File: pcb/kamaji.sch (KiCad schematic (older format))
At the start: 30 parts, among them J1 RJ10, J2 RJ10, J3 RJ10, J4 RJ10, J5 RJ10, Q1 IRF540N, SW1 CTRL1, SW2 CTRL2, SW3 CTRL3, U1 ATMEGA328P-PU

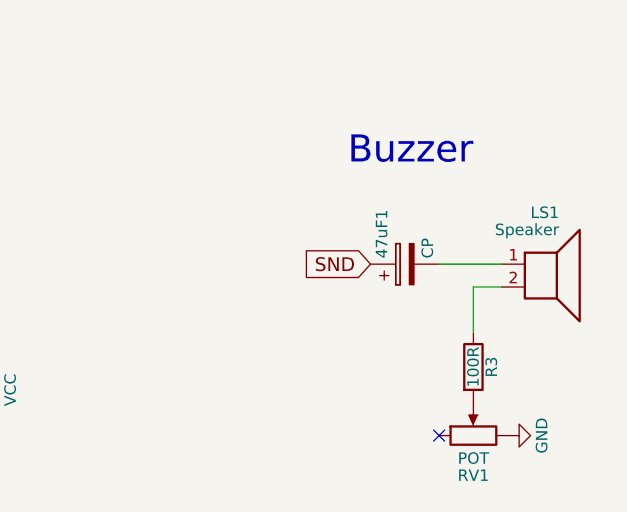
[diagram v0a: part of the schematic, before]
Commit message: fix the capacitor labels
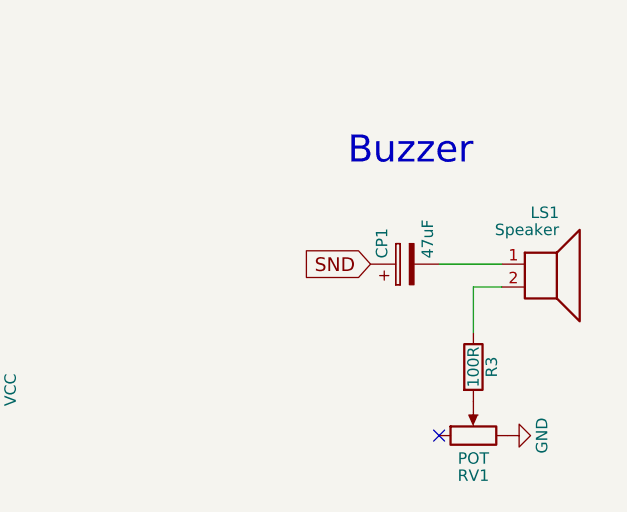
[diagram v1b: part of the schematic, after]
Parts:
- CP1: renamed from 47uF1; value CP -> 47uF
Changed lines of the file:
@@
 $EndComp
 $Comp
-L GND #PWR01
+L GND #PWR8
 U 1 1 596B2D5F
 P 2125 6925
-F 0 "#PWR01" H 2125 6675 50  0001 C CNN
+F 0 "#PWR8" H 2125 6675 50  0001 C CNN
 F 1 "GND" H 2125 6775 50  0000 C CNN
 F 2 "" H 2125 6925 50  0001 C CNN
@@
 $EndComp
 $Comp
-L GND #PWR02
+L GND #PWR7
 U 1 1 596B2D7D
 P 1950 6925
-F 0 "#PWR02" H 1950 6675 50  0001 C CNN
+F 0 "#PWR7" H 1950 6675 50  0001 C CNN
 F 1 "GND" H 1950 6775 50  0000 C CNN
 F 2 "" H 1950 6925 50  0001 C CNN
@@
 PBTN1
 $Comp
-L GND #PWR03
+L GND #PWR5
 U 1 1 596B3698
 P 1150 3925
-F 0 "#PWR03" H 1150 3675 50  0001 C CNN
+F 0 "#PWR5" H 1150 3675 50  0001 C CNN
 F 1 "GND" H 1150 3775 50  0000 C CNN
 F 2 "" H 1150 3925 50  0001 C CNN
@@
 $EndComp
 $Comp
-L VCC #PWR04
+L VCC #PWR32
 U 1 1 596B3963
 P 7275 4900
-F 0 "#PWR04" H 7275 4750 50  0001 C CNN
+F 0 "#PWR32" H 7275 4750 50  0001 C CNN
 F 1 "VCC" H 7275 5050 50  0000 C CNN
 F 2 "" H 7275 4900 50  0001 C CNN
@@
 $EndComp
 $Comp
-L VCC #PWR05
+L VCC #PWR6
 U 1 1 596B398D
 P 1175 1375
-F 0 "#PWR05" H 1175 1225 50  0001 C CNN
+F 0 "#PWR6" H 1175 1225 50  0001 C CNN
 F 1 "VCC" H 1175 1525 50  0000 C CNN
 F 2 "" H 1175 1375 50  0001 C CNN
@@
 $EndComp
 $Comp
-L GND #PWR06
+L GND #PWR30
 U 1 1 596B8372
 P 6975 5600
-F 0 "#PWR06" H 6975 5350 50  0001 C CNN
+F 0 "#PWR30" H 6975 5350 50  0001 C CNN
 F 1 "GND" H 6975 5450 50  0000 C CNN
 F 2 "" H 6975 5600 50  0001 C CNN
@@
 SND
 $Comp
-L GND #PWR07
+L GND #PWR35
 U 1 1 596BC371
 P 9650 5025
-F 0 "#PWR07" H 9650 4775 50  0001 C CNN
+F 0 "#PWR35" H 9650 4775 50  0001 C CNN
 F 1 "GND" H 9650 4875 50  0000 C CNN
 F 2 "" H 9650 5025 50  0001 C CNN
@@
 NoConn ~ 10050 4625
 $Comp
-L VCC #PWR08
+L VCC #PWR38
 U 1 1 596BC751
 P 10050 4425
-F 0 "#PWR08" H 10050 4275 50  0001 C CNN
+F 0 "#PWR38" H 10050 4275 50  0001 C CNN
 F 1 "VCC" H 10050 4575 50  0000 C CNN
 F 2 "" H 10050 4425 50  0001 C CNN
@@
 $EndComp
 $Comp
-L GND #PWR09
+L GND #PWR10
 U 1 1 596BE03C
 P 2875 5175
-F 0 "#PWR09" H 2875 4925 50  0001 C CNN
+F 0 "#PWR10" H 2875 4925 50  0001 C CNN
 F 1 "GND" H 2875 5025 50  0000 C CNN
 F 2 "" H 2875 5175 50  0001 C CNN
@@
 MOSI
 $Comp
-L VCC #PWR010
+L VCC #PWR9
 U 1 1 596BDF58
 P 2875 4850
-F 0 "#PWR010" H 2875 4700 50  0001 C CNN
+F 0 "#PWR9" H 2875 4700 50  0001 C CNN
 F 1 "VCC" H 2875 5000 50  0000 C CNN
 F 2 "" H 2875 4850 50  0001 C CNN
@@
 $EndComp
 $Comp
-L VCC #PWR011
+L VCC #PWR14
 U 1 1 596BDA9E
 P 4225 3400
-F 0 "#PWR011" H 4225 3250 50  0001 C CNN
+F 0 "#PWR14" H 4225 3250 50  0001 C CNN
 F 1 "VCC" H 4225 3550 50  0000 C CNN
 F 2 "" H 4225 3400 50  0001 C CNN
@@
 CBTN1
 $Comp
-L GND #PWR012
+L GND #PWR16
 U 1 1 596C3F76
 P 5125 4625
-F 0 "#PWR012" H 5125 4375 50  0001 C CNN
+F 0 "#PWR16" H 5125 4375 50  0001 C CNN
 F 1 "GND" H 5125 4475 50  0000 C CNN
 F 2 "" H 5125 4625 50  0001 C CNN
@@
 $EndComp
 $Comp
-L GND #PWR013
+L GND #PWR17
 U 1 1 596C4178
 P 5125 4925
-F 0 "#PWR013" H 5125 4675 50  0001 C CNN
+F 0 "#PWR17" H 5125 4675 50  0001 C CNN
 F 1 "GND" H 5125 4775 50  0000 C CNN
 F 2 "" H 5125 4925 50  0001 C CNN
@@
 $EndComp
 $Comp
-L GND #PWR014
+L GND #PWR18
 U 1 1 596C4256
 P 5125 5250
-F 0 "#PWR014" H 5125 5000 50  0001 C CNN
+F 0 "#PWR18" H 5125 5000 50  0001 C CNN
 F 1 "GND" H 5125 5100 50  0000 C CNN
 F 2 "" H 5125 5250 50  0001 C CNN
@@
 $EndComp
 $Comp
-L GND #PWR015
+L GND #PWR31
 U 1 1 596C4E9E
 P 7225 2550
-F 0 "#PWR015" H 7225 2300 50  0001 C CNN
+F 0 "#PWR31" H 7225 2300 50  0001 C CNN
 F 1 "GND" H 7225 2400 50  0000 C CNN
 F 2 "" H 7225 2550 50  0001 C CNN
@@
 $EndComp
 $Comp
-L VCC #PWR016
+L VCC #PWR24
 U 1 1 596C53E2
 P 5650 3025
-F 0 "#PWR016" H 5650 2875 50  0001 C CNN
+F 0 "#PWR24" H 5650 2875 50  0001 C CNN
 F 1 "VCC" H 5650 3175 50  0000 C CNN
 F 2 "" H 5650 3025 50  0001 C CNN
@@
 $EndComp
 $Comp
-L GND #PWR017
+L GND #PWR25
 U 1 1 596C542C
 P 5650 3325
-F 0 "#PWR017" H 5650 3075 50  0001 C CNN
+F 0 "#PWR25" H 5650 3075 50  0001 C CNN
 F 1 "GND" H 5650 3175 50  0000 C CNN
 F 2 "" H 5650 3325 50  0001 C CNN
@@
 $EndComp
 $Comp
-L VCC #PWR018
+L VCC #PWR3
 U 1 1 596C7BFC
 P 1000 2725
-F 0 "#PWR018" H 1000 2575 50  0001 C CNN
+F 0 "#PWR3" H 1000 2575 50  0001 C CNN
 F 1 "VCC" H 1000 2875 50  0000 C CNN
 F 2 "" H 1000 2725 50  0001 C CNN
@@
 $EndComp
 $Comp
-L VCC #PWR019
+L VCC #PWR21
 U 1 1 596C84D4
 P 5375 1850
-F 0 "#PWR019" H 5375 1700 50  0001 C CNN
+F 0 "#PWR21" H 5375 1700 50  0001 C CNN
 F 1 "VCC" H 5375 2000 50  0000 C CNN
 F 2 "" H 5375 1850 50  0001 C CNN
@@
 $EndComp
 $Comp
-L GND #PWR020
+L GND #PWR22
 U 1 1 596C866D
 P 5375 2150
-F 0 "#PWR020" H 5375 1900 50  0001 C CNN
+F 0 "#PWR22" H 5375 1900 50  0001 C CNN
 F 1 "GND" H 5375 2000 50  0000 C CNN
 F 2 "" H 5375 2150 50  0001 C CNN
@@
 $EndComp
 $Comp
-L VCC #PWR021
+L VCC #PWR26
 U 1 1 596C8F8A
 P 5825 2550
-F 0 "#PWR021" H 5825 2400 50  0001 C CNN
+F 0 "#PWR26" H 5825 2400 50  0001 C CNN
 F 1 "VCC" H 5825 2700 50  0000 C CNN
 F 2 "" H 5825 2550 50  0001 C CNN
@@
 $EndComp
 $Comp
-L GND #PWR022
+L GND #PWR27
 U 1 1 596CA14D
 P 6125 2550
-F 0 "#PWR022" H 6125 2300 50  0001 C CNN
+F 0 "#PWR27" H 6125 2300 50  0001 C CNN
 F 1 "GND" H 6125 2400 50  0000 C CNN
 F 2 "" H 6125 2550 50  0001 C CNN
@@
 USB in
 $Comp
-L GND #PWR023
+L GND #PWR23
 U 1 1 596D5901
 P 5625 2550
-F 0 "#PWR023" H 5625 2300 50  0001 C CNN
+F 0 "#PWR23" H 5625 2300 50  0001 C CNN
 F 1 "GND" H 5625 2400 50  0000 C CNN
 F 2 "" H 5625 2550 50  0001 C CNN
@@
 $EndComp
 $Comp
-L GND #PWR024
+L GND #PWR4
 U 1 1 596D65A9
 P 1000 3025
-F 0 "#PWR024" H 1000 2775 50  0001 C CNN
+F 0 "#PWR4" H 1000 2775 50  0001 C CNN
 F 1 "GND" H 1000 2875 50  0000 C CNN
 F 2 "" H 1000 3025 50  0001 C CNN
@@
 $EndComp
 $Comp
-L VCC #PWR025
+L VCC #PWR33
 U 1 1 596CDFF3
 P 7500 2800
-F 0 "#PWR025" H 7500 2650 50  0001 C CNN
+F 0 "#PWR33" H 7500 2650 50  0001 C CNN
 F 1 "VCC" H 7500 2950 50  0000 C CNN
 F 2 "" H 7500 2800 50  0001 C CNN
@@
 $EndComp
 $Comp
-L GND #PWR026
+L GND #PWR12
 U 1 1 596F6E3F
 P 3175 6925
-F 0 "#PWR026" H 3175 6675 50  0001 C CNN
+F 0 "#PWR12" H 3175 6675 50  0001 C CNN
 F 1 "GND" H 3175 6775 50  0000 C CNN
 F 2 "" H 3175 6925 50  0001 C CNN
@@
 $EndComp
 $Comp
-L GND #PWR027
+L GND #PWR11
 U 1 1 596F6E45
 P 3000 6925
-F 0 "#PWR027" H 3000 6675 50  0001 C CNN
+F 0 "#PWR11" H 3000 6675 50  0001 C CNN
 F 1 "GND" H 3000 6775 50  0000 C CNN
 F 2 "" H 3000 6925 50  0001 C CNN
@@
 $EndComp
 $Comp
-L GND #PWR028
+L GND #PWR15
 U 1 1 596F75A8
 P 4275 6925
-F 0 "#PWR028" H 4275 6675 50  0001 C CNN
+F 0 "#PWR15" H 4275 6675 50  0001 C CNN
 F 1 "GND" H 4275 6775 50  0000 C CNN
 F 2 "" H 4275 6925 50  0001 C CNN
@@
 $EndComp
 $Comp
-L GND #PWR029
+L GND #PWR13
 U 1 1 596F75AE
 P 4100 6925
-F 0 "#PWR029" H 4100 6675 50  0001 C CNN
+F 0 "#PWR13" H 4100 6675 50  0001 C CNN
 F 1 "GND" H 4100 6775 50  0000 C CNN
 F 2 "" H 4100 6925 50  0001 C CNN
@@
 $EndComp
 $Comp
-L GND #PWR030
+L GND #PWR20
 U 1 1 596F75C6
 P 5325 6925
-F 0 "#PWR030" H 5325 6675 50  0001 C CNN
+F 0 "#PWR20" H 5325 6675 50  0001 C CNN
 F 1 "GND" H 5325 6775 50  0000 C CNN
 F 2 "" H 5325 6925 50  0001 C CNN
@@
 $EndComp
 $Comp
-L GND #PWR031
+L GND #PWR19
 U 1 1 596F75CC
 P 5150 6925
-F 0 "#PWR031" H 5150 6675 50  0001 C CNN
+F 0 "#PWR19" H 5150 6675 50  0001 C CNN
 F 1 "GND" H 5150 6775 50  0000 C CNN
 F 2 "" H 5150 6925 50  0001 C CNN
@@
 $EndComp
 $Comp
-L GND #PWR032
+L GND #PWR29
 U 1 1 596F7760
 P 6350 6925
-F 0 "#PWR032" H 6350 6675 50  0001 C CNN
+F 0 "#PWR29" H 6350 6675 50  0001 C CNN
 F 1 "GND" H 6350 6775 50  0000 C CNN
 F 2 "" H 6350 6925 50  0001 C CNN
@@
 $EndComp
 $Comp
-L GND #PWR033
+L GND #PWR28
 U 1 1 596F7766
 P 6175 6925
-F 0 "#PWR033" H 6175 6675 50  0001 C CNN
+F 0 "#PWR28" H 6175 6675 50  0001 C CNN
 F 1 "GND" H 6175 6775 50  0000 C CNN
 F 2 "" H 6175 6925 50  0001 C CNN
@@
 	9750 5250 9750 5025
 $Comp
-L GND #PWR034
+L GND #PWR36
 U 1 1 596FB4DD
 P 9750 5650
-F 0 "#PWR034" H 9750 5400 50  0001 C CNN
+F 0 "#PWR36" H 9750 5400 50  0001 C CNN
 F 1 "GND" H 9750 5500 50  0000 C CNN
 F 2 "" H 9750 5650 50  0001 C CNN
@@
 $EndComp
 $Comp
-L VCC #PWR035
+L VCC #PWR1
 U 1 1 5970C412
 P 700 2725
-F 0 "#PWR035" H 700 2575 50  0001 C CNN
+F 0 "#PWR1" H 700 2575 50  0001 C CNN
 F 1 "VCC" H 700 2875 50  0000 C CNN
 F 2 "" H 700 2725 50  0001 C CNN
@@
 $EndComp
 $Comp
-L GND #PWR036
+L GND #PWR2
 U 1 1 5970C418
 P 700 3025
-F 0 "#PWR036" H 700 2775 50  0001 C CNN
+F 0 "#PWR2" H 700 2775 50  0001 C CNN
 F 1 "GND" H 700 2875 50  0000 C CNN
 F 2 "" H 700 3025 50  0001 C CNN
@@
 $EndComp
 $Comp
-L GND #PWR037
+L GND #PWR37
 U 1 1 5973B33C
 P 9825 3000
-F 0 "#PWR037" H 9825 2750 50  0001 C CNN
+F 0 "#PWR37" H 9825 2750 50  0001 C CNN
 F 1 "GND" H 9825 2850 50  0000 C CNN
 F 2 "" H 9825 3000 50  0001 C CNN
@@
 Connection ~ 9325 5500
 $Comp
-L GND #PWR038
+L GND #PWR34
 U 1 1 5973D38C
 P 9325 5850
-F 0 "#PWR038" H 9325 5600 50  0001 C CNN
+F 0 "#PWR34" H 9325 5600 50  0001 C CNN
 F 1 "GND" H 9325 5700 50  0000 C CNN
 F 2 "" H 9325 5850 50  0001 C CNN
@@
 $EndComp
 $Comp
-L CP 47uF1
+L CP CP1
 U 1 1 5973C6F5
 P 9375 2250
-F 0 "47uF1" H 9400 2350 50  0000 L CNN
-F 1 "CP" H 9400 2150 50  0000 L CNN
+F 0 "CP1" H 9400 2350 50  0000 L CNN
+F 1 "47uF" H 9400 2150 50  0000 L CNN
 F 2 "Capacitors_THT:CP_Radial_D4.0mm_P1.50mm" H 9413 2100 50  0001 C CNN
 F 3 "" H 9375 2250 50  0001 C CNN

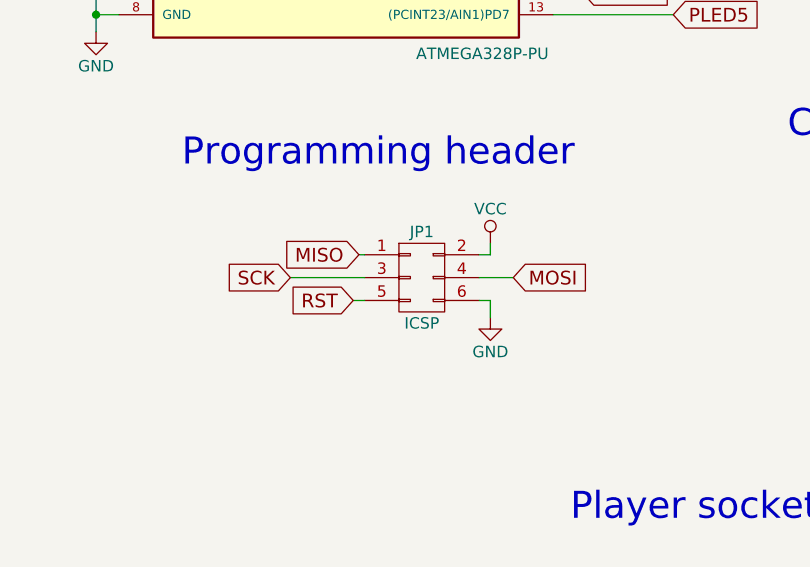
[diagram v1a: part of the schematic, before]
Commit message: switch to a 10-pin ICSP connector
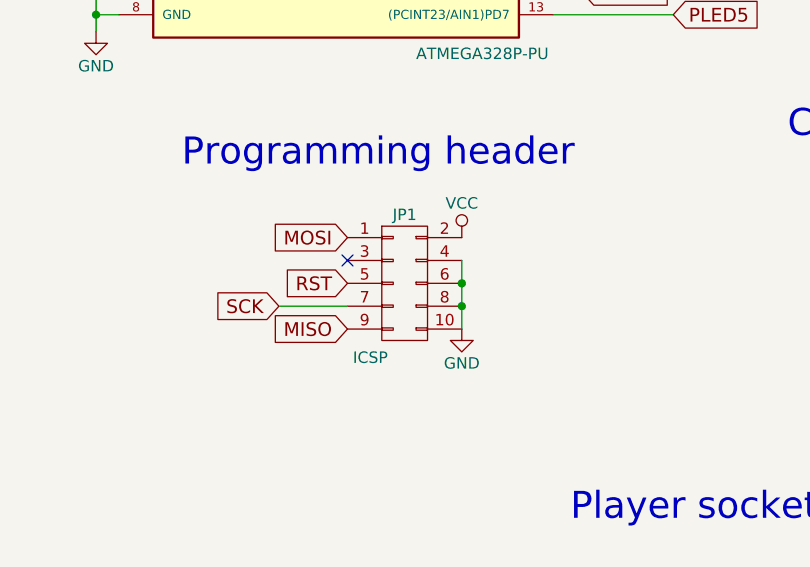
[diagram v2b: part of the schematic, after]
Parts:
- removed JP1: ICSP, Connectors:IDC_Header_Straight_6pins, symbol CONN_02X03
- added JP1: ICSP, Connectors:IDC_Header_Straight_10pins, symbol CONN_02X05
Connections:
- net CBTN2: now also JP1.1 (P1)
- net CBTN3: now also JP1.9 (P9)
- net GND: now also JP1.10 (P10), JP1.4 (P4), JP1.6 (P6), JP1.8 (P8)
- net RST: now also JP1.5 (P5)
- net SCK: now also JP1.7 (P7)
- net VCC: now also JP1.2 (P2)
- no-connect marks 9 -> 10

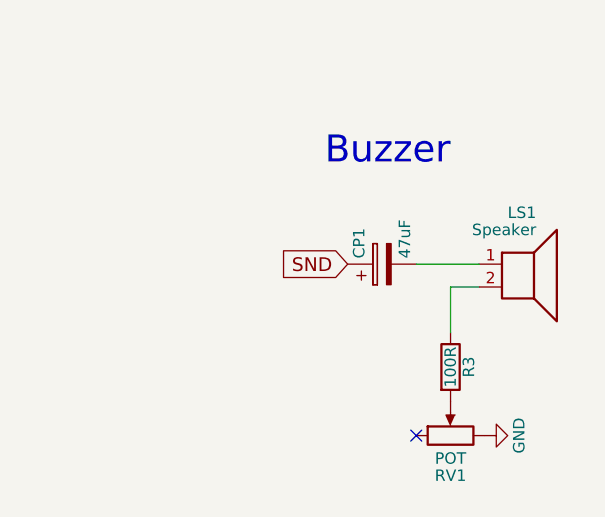
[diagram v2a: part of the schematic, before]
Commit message: change a capacitor value
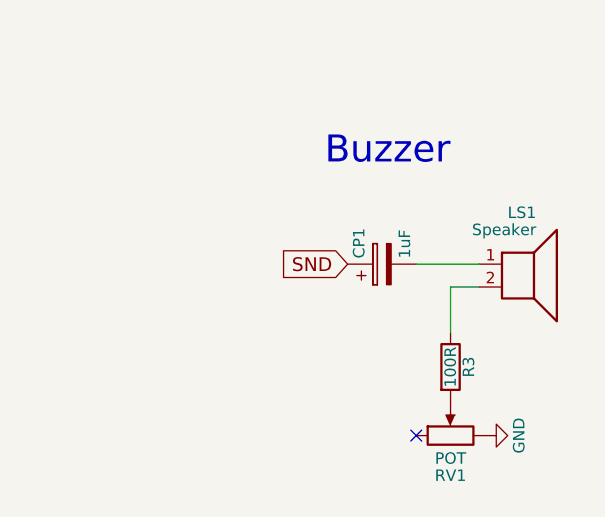
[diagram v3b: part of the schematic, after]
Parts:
- CP1: value 47uF -> 1uF
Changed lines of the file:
@@
 P 9375 2250
 F 0 "CP1" H 9400 2350 50  0000 L CNN
-F 1 "47uF" H 9400 2150 50  0000 L CNN
+F 1 "1uF" H 9400 2150 50  0000 L CNN
 F 2 "Capacitors_THT:CP_Radial_D4.0mm_P1.50mm" H 9413 2100 50  0001 C CNN
 F 3 "" H 9375 2250 50  0001 C CNN

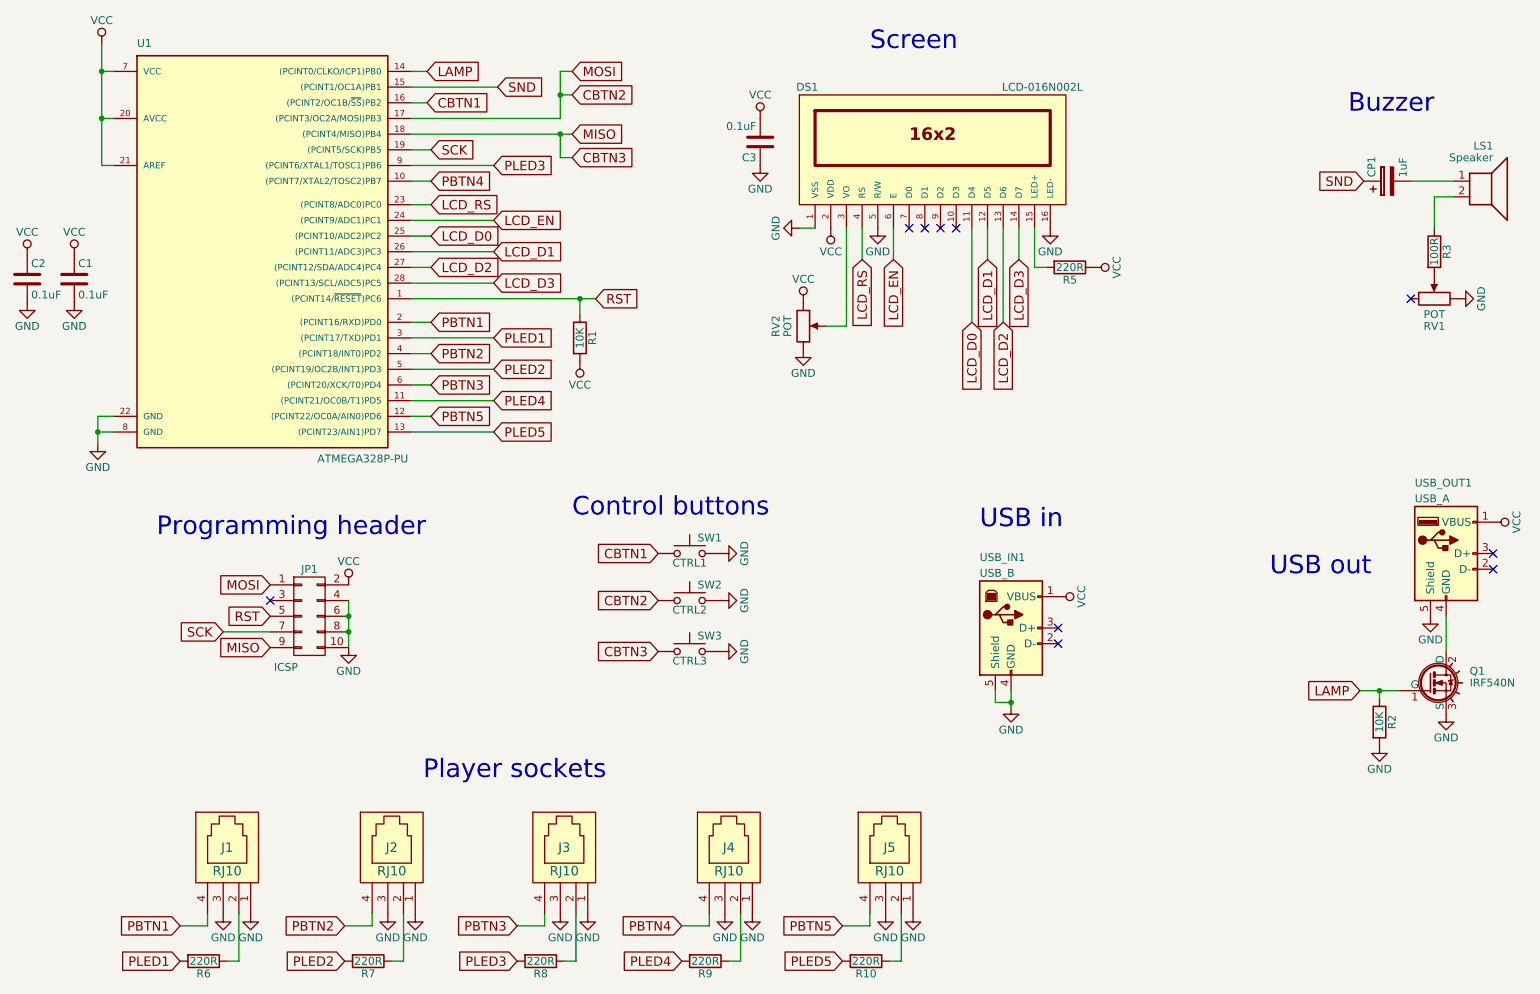
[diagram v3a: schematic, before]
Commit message: start laying out a new, smaller PCB
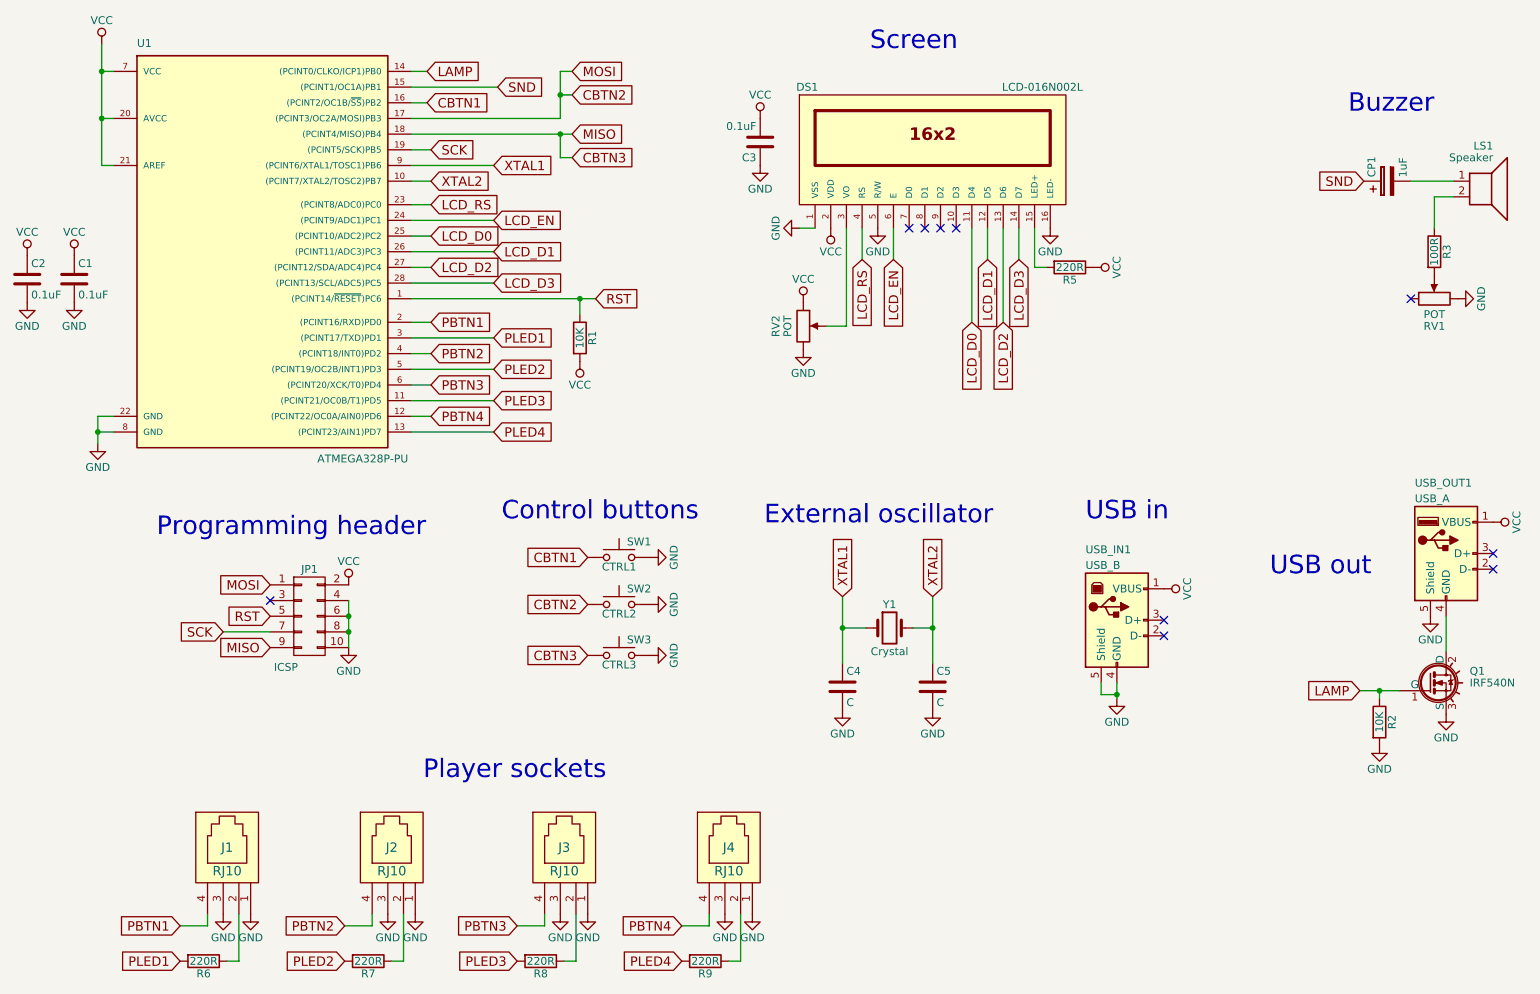
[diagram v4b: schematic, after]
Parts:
- removed J5: RJ10, kamaji:RJ10, symbol RJ10
- removed R10: 220R, Resistors_THT:R_Axial_DIN0207_L6.3mm_D2.5mm_P10.16mm_Horizontal, symbol R
- added C4, C5: C, Capacitors_THT:C_Disc_D3.8mm_W2.6mm_P2.50mm, symbol C
- added Y1: Crystal, Crystals:Crystal_HC49-U_Vertical, symbol Crystal
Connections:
- net PBTN5 is gone; now on net PBTN4: U1.12 ((PCINT22/OC0A/AIN0)PD6)
- net PLED5 is gone; now on net PLED4: U1.13 ((PCINT23/AIN1)PD7)
- net GND: now also C4.2, C5.2
- net PBTN4: no longer U1.10 ((PCINT7/XTAL2/TOSC2)PB7)
- net PLED3: now also U1.11 ((PCINT21/OC0B/T1)PD5); no longer U1.9 ((PCINT6/XTAL1/TOSC1)PB6)
- net PLED4: no longer U1.11 ((PCINT21/OC0B/T1)PD5)
- new net XTAL1: C4.1, U1.9 ((PCINT6/XTAL1/TOSC1)PB6), Y1.1
- new net XTAL2: C5.1, U1.10 ((PCINT7/XTAL2/TOSC2)PB7), Y1.2
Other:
- note added: "External oscillator"
- moved on the sheet: SW1, SW2, SW3, USB_IN1
